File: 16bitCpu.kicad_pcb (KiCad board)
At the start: 2 copper layers, 12 parts, among them U1 74LS245, U10 74LS245, U11 74LS173, U12 74LS173, U2 74LS173, U3 74LS173, U4 74LS245, U5 74LS173, U6 74LS173, U7 74LS245, U8 74LS173, U9 74LS173

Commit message: Added IR,Cu started
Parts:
- added C1: 0.01uF, Capacitor_THT:CP_Axial_L10.0mm_D4.5mm_P15.00mm_Horizontal, F.Cu at (204.5, 35.6)
- added C2: 1uF, Capacitor_THT:CP_Axial_L10.0mm_D4.5mm_P15.00mm_Horizontal, F.Cu at (171.9, 55.0)
- added C3: 0.01uF, Capacitor_THT:CP_Axial_L10.0mm_D4.5mm_P15.00mm_Horizontal, F.Cu at (171.9, 61.5)
- added C4: 0.1uF, Capacitor_THT:CP_Axial_L10.0mm_D4.5mm_P15.00mm_Horizontal, F.Cu at (190.5, 55.0)
- added C5: 0.01uF, Capacitor_THT:CP_Axial_L10.0mm_D4.5mm_P15.00mm_Horizontal, F.Cu at (171.9, 68.0)
- added C6: 0.01uF, Capacitor_THT:CP_Axial_L10.0mm_D4.5mm_P15.00mm_Horizontal, F.Cu at (38.4, 118.4)
- added R1: 1K, Resistor_THT:R_Axial_DIN0204_L3.6mm_D1.6mm_P7.62mm_Horizontal, F.Cu at (207.2, 59.6)
- added R2: 1K, Resistor_THT:R_Axial_DIN0204_L3.6mm_D1.6mm_P7.62mm_Horizontal, F.Cu at (208.7, 53.1)
- added R3: 1K, Resistor_THT:R_Axial_DIN0204_L3.6mm_D1.6mm_P7.62mm_Horizontal, F.Cu at (214.8, 46.5)
- added R4: 1M, Resistor_THT:R_Axial_DIN0204_L3.6mm_D1.6mm_P7.62mm_Horizontal, F.Cu at (214.8, 43.3)
- added R5: 1K, Resistor_THT:R_Axial_DIN0204_L3.6mm_D1.6mm_P7.62mm_Horizontal, F.Cu at (214.8, 40.2)
- added R6: 1K, Resistor_THT:R_Axial_DIN0204_L3.6mm_D1.6mm_P7.62mm_Horizontal, F.Cu at (208.7, 50.0)
- added R7: 1K, Resistor_THT:R_Axial_DIN0204_L3.6mm_D1.6mm_P7.62mm_Horizontal, F.Cu at (56.6, 116.4)
- added RV1: 1M, ROM:Potentiometer-5.5mm, F.Cu at (205.1, 46.0)
- added SW1: SW_Push, Button_Switch_THT:SW_PUSH-12mm, F.Cu at (191.0, 62.3)
- added SW2: SW_SPDT, ROM:DPDT-pushbutton, F.Cu at (217.9, 58.8)
- added U13: 74LS173, Package_DIP:DIP-16_W7.62mm, F.Cu at (137.7, 114.2)
- added U14: 74LS245, Package_DIP:DIP-20_W7.62mm, F.Cu at (137.7, 135.9)
- added U15: 74LS173, Package_DIP:DIP-16_W7.62mm, F.Cu at (137.7, 103.4)
- added U16: 74LS173, Package_DIP:DIP-16_W7.62mm, F.Cu at (137.7, 92.5)
- added U17: 74LS245, Package_DIP:DIP-20_W7.62mm, F.Cu at (183.6, 102.2)
- added U18: 74LS173, Package_DIP:DIP-16_W7.62mm, F.Cu at (161.0, 106.0)
- added U19: 74LS173, Package_DIP:DIP-16_W7.62mm, F.Cu at (216.2, 102.2)
- added U20: 74LS245, Package_DIP:DIP-20_W7.62mm, F.Cu at (194.4, 102.2)
- added U21: 74LS173, Package_DIP:DIP-16_W7.62mm, F.Cu at (205.3, 102.2)
- added U22: 74LS173, Package_DIP:DIP-16_W7.62mm, F.Cu at (171.8, 106.0)
- added U23: LM555xM, Package_SO:SOIC-8_3.9x4.9mm_P1.27mm, F.Cu at (210.0, 64.4)
- added U24: 74LS04, Package_DIP:DIP-14_W7.62mm, F.Cu at (160.9, 34.1)
- added U25: 74LS08, Package_DIP:DIP-14_W7.62mm, F.Cu at (160.9, 53.5)
- added U26: 74LS04, Package_DIP:DIP-14_W7.62mm, F.Cu at (171.8, 34.1)
- added U27: 74LS32, Package_DIP:DIP-14_W7.62mm, F.Cu at (182.6, 34.1)
- added U28: LM555xM, Package_SO:SOIC-8_3.9x4.9mm_P1.27mm, F.Cu at (222.0, 51.3)
- added U29: 74LS04, Package_DIP:DIP-14_W7.62mm, F.Cu at (193.5, 34.1)
- added U30: LM555xM, Package_SO:SOIC-8_3.9x4.9mm_P1.27mm, F.Cu at (225.5, 35.3)
- added U31: 74LS245, Package_DIP:DIP-20_W7.62mm, F.Cu at (127.5, 34.1)
- added U32: 74HC04, Package_DIP:DIP-14_W7.62mm, F.Cu at (149.2, 34.1)
- added U33: 74LS173, Package_DIP:DIP-16_W7.62mm, F.Cu at (101.6, 71.3)
- added U34: 74HC00, Package_DIP:DIP-14_W7.62mm, F.Cu at (90.7, 93.2)
- added U35: 74LS173, Package_DIP:DIP-16_W7.62mm, F.Cu at (90.7, 71.3)
- added U36: 74LS245, Package_DIP:DIP-20_W7.62mm, F.Cu at (138.4, 34.1)
- added U37: 74LS173, Package_DIP:DIP-16_W7.62mm, F.Cu at (127.5, 61.1)
- added U38: 74LS173, Package_DIP:DIP-16_W7.62mm, F.Cu at (112.4, 71.3)
- added U39: AS6C6264, Package_DIP:DIP-28_W15.24mm, F.Cu at (90.7, 34.1)
- added U40: AS6C6264, Package_DIP:DIP-28_W15.24mm, F.Cu at (109.1, 34.1)
- added U41: AT28C64B-15PU, ROM:3M_240-1280-00-0602J, F.Cu at (51.3, 79.4)
- added U42: AT28C64B-15PU, ROM:3M_240-1280-00-0602J, F.Cu at (76.9, 79.4)
- added U43: 74LS245, Package_DIP:DIP-20_W7.62mm, F.Cu at (160.9, 77.8)
- added U44: 74LS245, Package_DIP:DIP-20_W7.62mm, F.Cu at (171.8, 77.8)
- added U45: 74LS161, Package_DIP:DIP-16_W7.62mm, F.Cu at (182.6, 77.8)
- added U46: 74LS161, Package_DIP:DIP-16_W7.62mm, F.Cu at (193.5, 77.8)
- added U47: 74LS161, Package_DIP:DIP-16_W7.62mm, F.Cu at (204.3, 77.8)
- added U48: 74LS161, Package_DIP:DIP-16_W7.62mm, F.Cu at (215.2, 77.8)
- U10, U7: value 74LS245 -> 74LS86; footprint Package_DIP:DIP-20_W7.62mm -> Package_DIP:DIP-14_W7.62mm
- U11, U2: value 74LS173 -> 74LS245; footprint Package_DIP:DIP-16_W7.62mm -> Package_DIP:DIP-20_W7.62mm
- U3, U5, U6: value 74LS173 -> 74LS283
- U4: value 74LS245 -> 74LS283; footprint Package_DIP:DIP-20_W7.62mm -> Package_DIP:DIP-16_W7.62mm
- U8, U9: value 74LS173 -> 74LS86; footprint Package_DIP:DIP-16_W7.62mm -> Package_DIP:DIP-14_W7.62mm
- moved U4 106.4 mm to (113.6, 137.5), turned to 90 degrees
- moved U5 105.4 mm to (113.6, 148.3), turned to 90 degrees
- moved U3 98.7 mm to (88.5, 143.3), turned to 90 degrees
- moved U2 97.2 mm to (57.7, 140.8), turned to 90 degrees
- moved U1 85.5 mm to (57.7, 130.0), turned to 90 degrees
- moved U6 82.4 mm to (113.6, 126.7), turned to 90 degrees
- moved U11 74.1 mm to (137.7, 146.8), turned to 90 degrees
- moved U7 59.2 mm to (88.5, 132.4), turned to 90 degrees
- moved U8 50.4 mm to (113.6, 115.8), turned to 90 degrees
- moved U12 50.4 mm to (137.7, 125.1), turned to 90 degrees
- moved U10 43.9 mm to (88.5, 121.6), turned to 90 degrees
- moved U9 35.3 mm to (113.6, 105.0), turned to 90 degrees
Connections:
- U1 pad 11: /register b/Bus5 -> /ALU/BUS7
- U1 pad 12: /register b/Bus6 -> /ALU/BUS6
- U1 pad 13: /register b/Bus5 -> /ALU/BUS5
- U1 pad 14: /register b/Bus4 -> /ALU/BUS4
- U1 pad 15: /register b/Bus12 -> /ALU/BUS3
- U1 pad 16: /register b/Bus2 -> /ALU/BUS2
- U1 pad 17: /register b/Bus1 -> /ALU/BUS1
- U1 pad 18: /register b/Bus0 -> /ALU/BUS0
- U1 pad 19: /resgister/AO -> /ALU/~EO
- U10 pad 1: +5V -> /sheet5F747766/A12
- U10 pad 10: GND -> /ALU/SU
- U10 pad 11: /register b/Bus15 -> Net-(U10-Pad11)
- U10 pad 12: /register b/Bus14 -> /sheet5F747766/A15
- U10 pad 13: /register b/Bus13 -> /ALU/SU
- U10 pad 14: /register b/Bus12 -> (no net)
- U10 pad 2: Net-(U10-Pad2) -> /ALU/SU
- U10 pad 4: Net-(U10-Pad4) -> /sheet5F747766/A13
- U10 pad 5: Net-(U10-Pad5) -> /ALU/SU
- U10 pad 7: Net-(U10-Pad7) -> (no net)
- U10 pad 9: Net-(U10-Pad9) -> /sheet5F747766/A14
- U11 pad 1: GND -> +5V
- U11 pad 10: /register b/AI -> GND
- U11 pad 11: /register b/Bus11 -> /ALU/BUS7
- U11 pad 12: /register b/Bus10 -> /ALU/BUS6
- U11 pad 13: /register b/Bus9 -> /ALU/BUS5
- U11 pad 14: /register b/Bus8 -> /ALU/BUS4
- U11 pad 15: /register b/CLR -> /ALU/BUS3
- U11 pad 16: +5V -> /ALU/BUS2
- U11 pad 2: GND -> /ALU/A0
- U11 pad 3: Net-(U10-Pad2) -> /ALU/A1
- U11 pad 4: Net-(U10-Pad3) -> /ALU/A2
- U11 pad 5: Net-(U10-Pad4) -> /ALU/A3
- U11 pad 6: Net-(U10-Pad5) -> /ALU/A4
- U11 pad 7: /register b/CLK -> /ALU/A5
- U11 pad 8: GND -> /ALU/A6
- U11 pad 9: /register b/AI -> /ALU/A7
- U12 pad 10: /register b/AI -> /Resgister A/~AI
- U12 pad 11: /register b/Bus15 -> /ALU/BUS3
- U12 pad 12: /register b/Bus14 -> /ALU/BUS2
- U12 pad 13: /register b/Bus13 -> /ALU/BUS1
- U12 pad 14: /register b/Bus12 -> /ALU/BUS0
- U12 pad 15: /register b/CLR -> /Resgister A/CLR
- U12 pad 3: Net-(U10-Pad6) -> /ALU/A0
- U12 pad 4: Net-(U10-Pad7) -> /ALU/A1
- U12 pad 5: Net-(U10-Pad8) -> /ALU/A2
- U12 pad 6: Net-(U10-Pad9) -> /ALU/A3
- U12 pad 7: /register b/CLK -> /ProgramCounter/CLK
- U12 pad 9: /register b/AI -> /Resgister A/~AI
- U2 pad 1: GND -> +5V
- U2 pad 10: /resgister/AI -> GND
- U2 pad 11: /register b/Bus12 -> /ALU/BUS13
- U2 pad 12: /register b/Bus2 -> /ALU/BUS14
- U2 pad 13: /register b/Bus1 -> /ALU/BUS13
- U2 pad 14: /register b/Bus0 -> /ALU/BUS12
- U2 pad 15: /resgister/CLR -> /ALU/BUS11
- U2 pad 16: +5V -> /ALU/BUS10
- U2 pad 2: GND -> Net-(U2-Pad2)
- U2 pad 3: Net-(U1-Pad2) -> Net-(U2-Pad3)
- U2 pad 4: Net-(U1-Pad3) -> Net-(U2-Pad4)
- U2 pad 5: Net-(U1-Pad4) -> Net-(U2-Pad5)
- U2 pad 6: Net-(U1-Pad5) -> Net-(U2-Pad6)
- U2 pad 7: /resgister/CLK -> Net-(U2-Pad7)
- U2 pad 8: GND -> Net-(U2-Pad8)
- U2 pad 9: /resgister/AI -> Net-(U2-Pad9)
- U3 pad 1: GND -> Net-(U1-Pad3)
- U3 pad 10: /resgister/AI -> Net-(U1-Pad5)
- U3 pad 11: /register b/Bus5 -> Net-(U3-Pad11)
- U3 pad 12: /register b/Bus6 -> /ALU/A3
- U3 pad 13: /register b/Bus5 -> Net-(U1-Pad4)
- U3 pad 14: /register b/Bus4 -> /ALU/A2
- U3 pad 15: /resgister/CLR -> Net-(U3-Pad15)
- U3 pad 2: GND -> Net-(U3-Pad2)
- U3 pad 3: Net-(U1-Pad6) -> /ALU/A1
- U3 pad 4: Net-(U1-Pad7) -> Net-(U1-Pad2)
- U3 pad 5: Net-(U1-Pad8) -> /ALU/A0
- U3 pad 6: Net-(U1-Pad9) -> Net-(U3-Pad6)
- U3 pad 7: /resgister/CLK -> /ALU/SU
- U3 pad 9: /resgister/AI -> Net-(U3-Pad9)
- U4 pad 1: +5V -> Net-(U2-Pad3)
- U4 pad 10: GND -> Net-(U2-Pad5)
- U4 pad 11: /register b/Bus15 -> Net-(U4-Pad11)
- U4 pad 12: /register b/Bus14 -> /ALU/A11
- U4 pad 13: /register b/Bus13 -> Net-(U2-Pad4)
- U4 pad 14: /register b/Bus12 -> /ALU/A10
- U4 pad 15: /register b/Bus11 -> Net-(U4-Pad15)
- U4 pad 16: /register b/Bus10 -> +5V
- U4 pad 3: Net-(U4-Pad3) -> /ALU/A9
- U4 pad 4: Net-(U4-Pad4) -> Net-(U2-Pad2)
- U4 pad 5: Net-(U4-Pad5) -> /ALU/A8
- U4 pad 8: Net-(U4-Pad8) -> GND
- U5 pad 1: GND -> Net-(U1-Pad7)
- U5 pad 10: /resgister/AI -> Net-(U1-Pad9)
- U5 pad 11: /register b/Bus11 -> Net-(U5-Pad11)
- U5 pad 12: /register b/Bus10 -> /ALU/A7
- U5 pad 13: /register b/Bus9 -> Net-(U1-Pad8)
- U5 pad 14: /register b/Bus8 -> /ALU/A6
- U5 pad 15: /resgister/CLR -> Net-(U5-Pad15)
- U5 pad 2: GND -> Net-(U5-Pad2)
- U5 pad 3: Net-(U4-Pad2) -> /ALU/A5
- U5 pad 4: Net-(U4-Pad3) -> Net-(U1-Pad6)
- U5 pad 5: Net-(U4-Pad4) -> /ALU/A4
- U5 pad 6: Net-(U4-Pad5) -> Net-(U5-Pad6)
- U5 pad 7: /resgister/CLK -> Net-(U3-Pad9)
- U5 pad 9: /resgister/AI -> Net-(U4-Pad7)
- U6 pad 1: GND -> Net-(U2-Pad7)
- U6 pad 10: /resgister/AI -> Net-(U2-Pad9)
- U6 pad 11: /register b/Bus15 -> Net-(U10-Pad11)
- U6 pad 12: /register b/Bus14 -> /ALU/A15
- U6 pad 13: /register b/Bus13 -> Net-(U2-Pad8)
- U6 pad 14: /register b/Bus12 -> /ALU/A14
- U6 pad 15: /resgister/CLR -> Net-(U10-Pad8)
- U6 pad 2: GND -> Net-(U10-Pad6)
- U6 pad 3: Net-(U4-Pad6) -> /ALU/A13
- U6 pad 4: Net-(U4-Pad7) -> Net-(U2-Pad6)
- U6 pad 5: Net-(U4-Pad8) -> /ALU/A12
- U6 pad 6: Net-(U4-Pad9) -> Net-(U10-Pad3)
- U6 pad 7: /resgister/CLK -> Net-(U4-Pad9)
- U6 pad 9: /resgister/AI -> (no net)
- U7 pad 1: +5V -> /sheet5F747766/A0
- U7 pad 10: GND -> /ALU/SU
- U7 pad 11: /register b/Bus5 -> Net-(U3-Pad11)
- U7 pad 12: /register b/Bus6 -> /sheet5F747766/A3
- U7 pad 13: /register b/Bus5 -> /ALU/SU
- U7 pad 14: /register b/Bus4 -> (no net)
- U7 pad 2: Net-(U7-Pad2) -> /ALU/SU
- U7 pad 3: Net-(U7-Pad3) -> Net-(U3-Pad6)
- U7 pad 4: Net-(U7-Pad4) -> /sheet5F747766/A1
- U7 pad 5: Net-(U7-Pad5) -> /ALU/SU
- U7 pad 6: Net-(U7-Pad6) -> Net-(U3-Pad2)
- U7 pad 7: Net-(U7-Pad7) -> (no net)
- U7 pad 8: Net-(U7-Pad8) -> Net-(U3-Pad15)
- U7 pad 9: Net-(U7-Pad9) -> /sheet5F747766/A2
- U8 pad 1: GND -> /sheet5F747766/A4
- U8 pad 10: /register b/AI -> /ALU/SU
- U8 pad 11: /register b/Bus12 -> Net-(U5-Pad11)
- U8 pad 12: /register b/Bus2 -> /sheet5F747766/A7
- U8 pad 13: /register b/Bus1 -> /ALU/SU
- U8 pad 14: /register b/Bus0 -> (no net)
- U8 pad 2: GND -> /ALU/SU
- U8 pad 3: Net-(U7-Pad2) -> Net-(U5-Pad6)
- U8 pad 4: Net-(U7-Pad3) -> /sheet5F747766/A5
- U8 pad 5: Net-(U7-Pad4) -> /ALU/SU
- U8 pad 6: Net-(U7-Pad5) -> Net-(U5-Pad2)
- U8 pad 7: /register b/CLK -> (no net)
- U8 pad 8: GND -> Net-(U5-Pad15)
- U8 pad 9: /register b/AI -> /sheet5F747766/A6
- U9 pad 1: GND -> /sheet5F747766/A8
- U9 pad 10: /register b/AI -> /ALU/SU
- U9 pad 11: /register b/Bus5 -> Net-(U4-Pad11)
- U9 pad 12: /register b/Bus6 -> /sheet5F747766/A11
- U9 pad 13: /register b/Bus5 -> /ALU/SU
- U9 pad 14: /register b/Bus4 -> (no net)
- U9 pad 2: GND -> /ALU/SU
- U9 pad 3: Net-(U7-Pad6) -> Net-(U4-Pad6)
- U9 pad 4: Net-(U7-Pad7) -> /sheet5F747766/A9
- U9 pad 5: Net-(U7-Pad8) -> /ALU/SU
- U9 pad 6: Net-(U7-Pad9) -> Net-(U4-Pad2)
- U9 pad 7: /register b/CLK -> (no net)
- U9 pad 8: GND -> Net-(U4-Pad15)
- U9 pad 9: /register b/AI -> /sheet5F747766/A10
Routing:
- net GND: track 0.00 -> 793.5 mm
- net +5V: track 0.00 -> 678.2 mm
- net /ALU/BUS12: track 0.00 -> 433.3 mm, vias 0 -> 1
- net /ALU/BUS13: track 0.00 -> 427.8 mm, vias 0 -> 1
- net /ALU/BUS8: track 0.00 -> 398.9 mm, vias 0 -> 1
- net /ALU/BUS14: track 0.00 -> 395.8 mm
- net /ALU/BUS5: track 0.00 -> 395.0 mm, vias 0 -> 3
- net /ALU/BUS10: track 0.00 -> 382.4 mm, vias 0 -> 3
- net /ALU/BUS6: track 0.00 -> 377.8 mm, vias 0 -> 2
- net /ALU/BUS11: track 0.00 -> 377.0 mm
- net /ALU/BUS9: track 0.00 -> 375.2 mm, vias 0 -> 1
- net /ALU/BUS4: track 0.00 -> 353.2 mm, vias 0 -> 5
- net /ProgramCounter/CLK: track 0.00 -> 351.4 mm
- net /ALU/BUS7: track 0.00 -> 346.4 mm, vias 0 -> 1
- net /ALU/BUS0: track 0.00 -> 338.1 mm
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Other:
- copper layers 2 -> 4

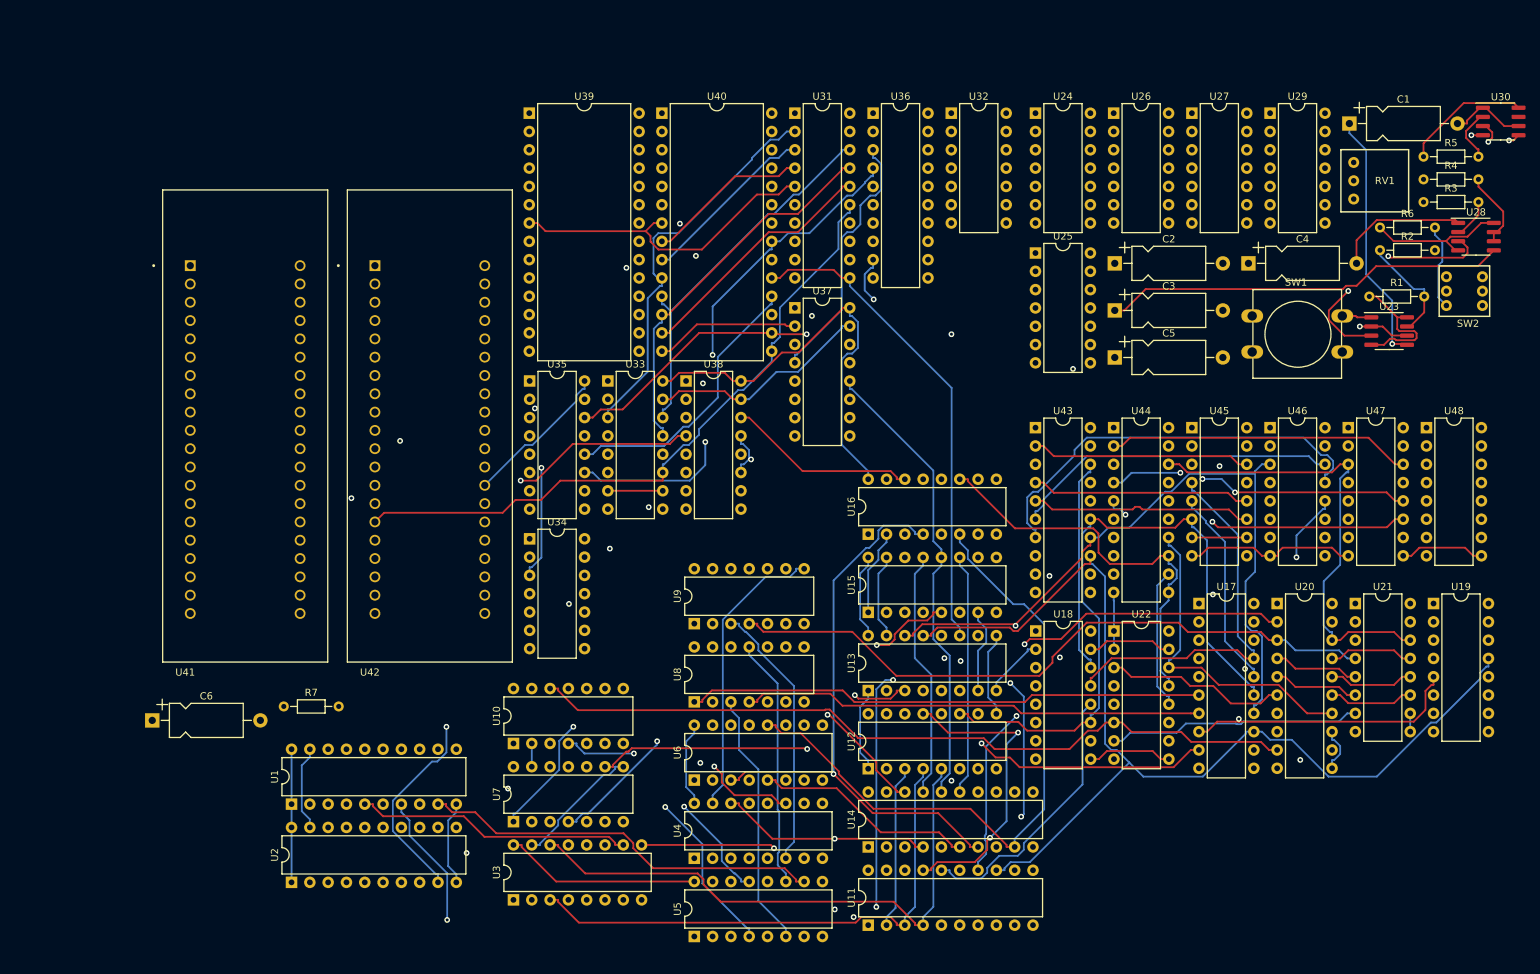
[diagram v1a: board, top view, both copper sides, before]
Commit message: Fixed power for multi part comps
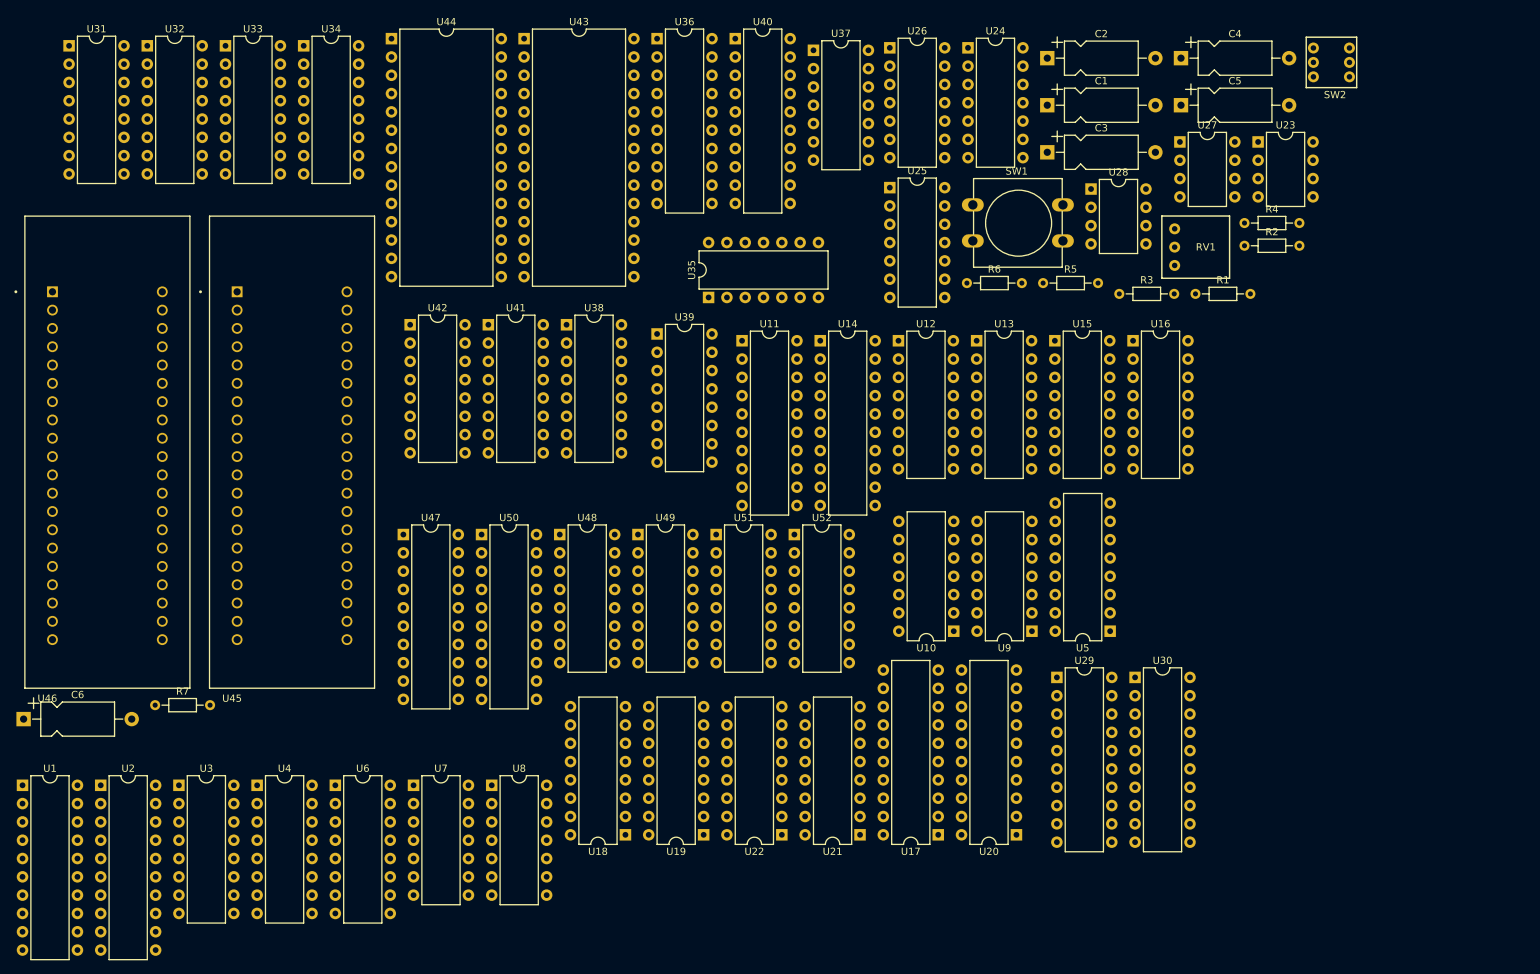
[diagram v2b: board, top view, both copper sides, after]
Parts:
- removed the U48 at (215.2, 77.8)
- added R4: 1M, Resistor_THT:R_Axial_DIN0204_L3.6mm_D1.6mm_P7.62mm_Horizontal, F.Cu at (189.9, 49.4)
- added U49: 74LS173, Package_DIP:DIP-16_W7.62mm, F.Cu at (105.8, 92.6)
- added U50: 74LS245, Package_DIP:DIP-20_W7.62mm, F.Cu at (84.1, 92.6)
- added U51: 74LS173, Package_DIP:DIP-16_W7.62mm, F.Cu at (116.6, 92.6)
- added U52: 74LS173, Package_DIP:DIP-16_W7.62mm, F.Cu at (127.5, 92.6)
- U23, U28: value LM555xM -> LM555xN; footprint Package_SO:SOIC-8_3.9x4.9mm_P1.27mm -> Package_DIP:DIP-8_W7.62mm
- U24, U26: value 74LS04 -> 74LS08
- U27: value 74LS32 -> LM555xN; footprint Package_DIP:DIP-14_W7.62mm -> Package_DIP:DIP-8_W7.62mm
- U29: value 74LS04 -> 74LS245; footprint Package_DIP:DIP-14_W7.62mm -> Package_DIP:DIP-20_W7.62mm
- U30: value LM555xM -> 74LS245; footprint Package_SO:SOIC-8_3.9x4.9mm_P1.27mm -> Package_DIP:DIP-20_W7.62mm
- U31: value 74LS245 -> 74LS161; footprint Package_DIP:DIP-20_W7.62mm -> Package_DIP:DIP-16_W7.62mm
- U32: value 74HC04 -> 74LS161; footprint Package_DIP:DIP-14_W7.62mm -> Package_DIP:DIP-16_W7.62mm
- U33: value 74LS173 -> 74LS161
- U34: value 74HC00 -> 74LS161; footprint Package_DIP:DIP-14_W7.62mm -> Package_DIP:DIP-16_W7.62mm
- U35: value 74LS173 -> 74HC00; footprint Package_DIP:DIP-16_W7.62mm -> Package_DIP:DIP-14_W7.62mm
- U37: value 74LS173 -> 74HC04; footprint Package_DIP:DIP-16_W7.62mm -> Package_DIP:DIP-14_W7.62mm
- U39: value AS6C6264 -> 74LS173; footprint Package_DIP:DIP-28_W15.24mm -> Package_DIP:DIP-16_W7.62mm
- U40: value AS6C6264 -> 74LS245; footprint Package_DIP:DIP-28_W15.24mm -> Package_DIP:DIP-20_W7.62mm
- U41, U42: value AT28C64B-15PU -> 74LS173; footprint ROM:3M_240-1280-00-0602J -> Package_DIP:DIP-16_W7.62mm
- U43, U44: value 74LS245 -> AS6C6264; footprint Package_DIP:DIP-20_W7.62mm -> Package_DIP:DIP-28_W15.24mm
- U45, U46: value 74LS161 -> AT28C64B-15PU; footprint Package_DIP:DIP-16_W7.62mm -> ROM:3M_240-1280-00-0602J
- U47: value 74LS161 -> 74LS245; footprint Package_DIP:DIP-16_W7.62mm -> Package_DIP:DIP-20_W7.62mm
- U48: renamed from R4; value 1M -> 74LS173; footprint Resistor_THT:R_Axial_DIN0204_L3.6mm_D1.6mm_P7.62mm_Horizontal -> Package_DIP:DIP-16_W7.62mm
- moved U46 161.4 mm to (32.2, 83.0)
- moved U47 131.9 mm to (73.2, 92.6)
- moved U48 129.6 mm to (94.9, 92.6)
- moved U45 125.0 mm to (57.8, 83.0)
- moved U44 113.8 mm to (71.6, 23.8)
- moved U32 111.9 mm to (37.7, 24.8)
- moved U19 106.2 mm to (114.9, 134.2), turned to 180 degrees
- moved U31 101.1 mm to (26.8, 24.8)
- moved U30 92.3 mm to (174.7, 112.4)
- moved U43 89.1 mm to (90.0, 23.8)
- moved U29 83.7 mm to (163.9, 112.4)
- moved U11 83.0 mm to (120.2, 65.7), turned to 0 degrees
- moved U21 75.8 mm to (136.6, 134.2), turned to 180 degrees
- moved U34 75.2 mm to (59.4, 24.8)
- moved U5 71.6 mm to (171.3, 106.0), turned to 180 degrees
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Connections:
- RV1 pad 3: (no net) -> Net-(RV1-Pad3)
- U10 pad 14: (no net) -> +5V
- U10 pad 7: (no net) -> GND
- U12 pad 7: /ProgramCounter/CLK -> /Control Unit/CLK
- U13 pad 7: /ProgramCounter/CLK -> /Control Unit/CLK
- U14 pad 11: /ALU/BUS13 -> /ALU/BUS15
- U15 pad 7: /ProgramCounter/CLK -> /Control Unit/CLK
- U16 pad 11: /ALU/BUS13 -> /ALU/BUS15
- U16 pad 7: /ProgramCounter/CLK -> /Control Unit/CLK
- U18 pad 7: /ProgramCounter/CLK -> /Control Unit/CLK
- U19 pad 7: /ProgramCounter/CLK -> /Control Unit/CLK
- U2 pad 11: /ALU/BUS13 -> /ALU/BUS15
- U20 pad 11: /ALU/BUS13 -> /ALU/BUS15
- U21 pad 7: /ProgramCounter/CLK -> /Control Unit/CLK
- U22 pad 11: /ALU/BUS13 -> /ALU/BUS15
- U22 pad 7: /ProgramCounter/CLK -> /Control Unit/CLK
- U24 pad 14: (no net) -> +5V
- U24 pad 3: (no net) -> /clock/HLT
- U24 pad 4: (no net) -> Net-(U24-Pad4)
- U24 pad 5: (no net) -> /Control Unit/CLK
- U24 pad 6: (no net) -> /clock/~CLK
- U24 pad 7: (no net) -> GND
- U25 pad 10: Net-(U25-Pad10) -> Net-(U24-Pad4)
- U25 pad 14: (no net) -> +5V
- U25 pad 7: (no net) -> GND
- U25 pad 8: /ProgramCounter/CLK -> /Control Unit/CLK
- U26 pad 1: (no net) -> Net-(U25-Pad3)
- U26 pad 14: (no net) -> +5V
- U26 pad 2: Net-(U25-Pad10) -> Net-(U25-Pad6)
- U26 pad 3: (no net) -> Net-(U25-Pad9)
- U26 pad 7: (no net) -> GND
- U27 pad 1: Net-(U25-Pad3) -> GND
- U27 pad 2: Net-(U25-Pad6) -> Net-(R3-Pad2)
- U27 pad 3: Net-(U25-Pad9) -> Net-(U25-Pad5)
- U27 pad 4: (no net) -> +5V
- U27 pad 5: (no net) -> Net-(C3-Pad1)
- U27 pad 6: (no net) -> Net-(C4-Pad1)
- U27 pad 7: (no net) -> Net-(C4-Pad1)
- U27 pad 8: (no net) -> +5V
- U28 pad 2: Net-(R3-Pad2) -> Net-(R5-Pad2)
- U28 pad 3: Net-(U25-Pad5) -> Net-(U24-Pad1)
- U28 pad 4: +5V -> Net-(R6-Pad2)
- U28 pad 5: Net-(C3-Pad1) -> Net-(C5-Pad1)
- U28 pad 6: Net-(C4-Pad1) -> GND
- U28 pad 7: Net-(C4-Pad1) -> Net-(U28-Pad7)
- U29 pad 1: /ProgramCounter/CLK -> +5V
- U29 pad 10: (no net) -> GND
- U29 pad 11: (no net) -> /ALU/BUS7
- U29 pad 12: (no net) -> /ALU/BUS6
- U29 pad 13: (no net) -> /ALU/BUS5
- U29 pad 14: (no net) -> /ALU/BUS4
- U29 pad 2: (no net) -> Net-(U29-Pad2)
- U29 pad 3: (no net) -> Net-(U29-Pad3)
- U29 pad 4: (no net) -> Net-(U29-Pad4)
- U29 pad 5: (no net) -> Net-(U29-Pad5)
- U29 pad 6: (no net) -> Net-(U29-Pad6)
- U29 pad 7: (no net) -> Net-(U29-Pad7)
- U29 pad 8: (no net) -> Net-(U29-Pad8)
- U29 pad 9: (no net) -> Net-(U29-Pad9)
- U30 pad 1: GND -> +5V
- U30 pad 2: Net-(R5-Pad2) -> Net-(U30-Pad2)
- U30 pad 3: Net-(U24-Pad1) -> Net-(U30-Pad3)
- U30 pad 4: Net-(R6-Pad2) -> Net-(U30-Pad4)
- U30 pad 5: Net-(C5-Pad1) -> Net-(U30-Pad5)
- U30 pad 6: GND -> Net-(U30-Pad6)
- U30 pad 7: (no net) -> Net-(U30-Pad7)
- U30 pad 8: +5V -> Net-(U30-Pad8)
- U31 pad 1: +5V -> /ProgramCounter/~CLR
- U31 pad 10: GND -> /ProgramCounter/CE
- U31 pad 11: /ALU/BUS7 -> Net-(U29-Pad5)
- U31 pad 12: /ALU/BUS6 -> Net-(U29-Pad4)
- U31 pad 13: /ALU/BUS5 -> Net-(U29-Pad3)
- U31 pad 14: /ALU/BUS4 -> Net-(U29-Pad2)
- U31 pad 15: /ALU/BUS3 -> Net-(U31-Pad15)
- U31 pad 16: /ALU/BUS2 -> +5V
- U31 pad 2: Net-(U31-Pad2) -> /Control Unit/CLK
- U31 pad 3: Net-(U31-Pad3) -> /ALU/BUS0
- U31 pad 4: Net-(U31-Pad4) -> /ALU/BUS1
- U31 pad 5: Net-(U31-Pad5) -> /ALU/BUS2
- U31 pad 6: Net-(U31-Pad6) -> /ALU/BUS3
- U31 pad 7: Net-(U31-Pad7) -> /ProgramCounter/CE
- U31 pad 8: Net-(U31-Pad8) -> GND
- U31 pad 9: Net-(U31-Pad9) -> /ProgramCounter/~J
- U32 pad 1: /ProgramCounter/CLK -> /ProgramCounter/~CLR
- U32 pad 10: (no net) -> /ProgramCounter/CE
- U32 pad 11: (no net) -> Net-(U29-Pad9)
- U32 pad 12: (no net) -> Net-(U29-Pad8)
- U32 pad 13: (no net) -> Net-(U29-Pad7)
- U32 pad 14: (no net) -> Net-(U29-Pad6)
- U32 pad 2: Net-(U32-Pad2) -> Net-(U31-Pad15)
- U32 pad 3: Net-(U32-Pad2) -> /ALU/BUS4
- U32 pad 4: Net-(C6-Pad1) -> /ALU/BUS5
- U32 pad 5: (no net) -> /ALU/BUS6
- U32 pad 6: (no net) -> /ALU/BUS7
- U32 pad 7: (no net) -> /ProgramCounter/CE
- U32 pad 8: (no net) -> GND
- U32 pad 9: (no net) -> /ProgramCounter/~J
- U33 pad 1: GND -> /ProgramCounter/~CLR
- U33 pad 10: /ProgramCounter/CLK -> /ProgramCounter/CE
- U33 pad 11: /ALU/BUS3 -> Net-(U30-Pad5)
- U33 pad 12: /ALU/BUS2 -> Net-(U30-Pad4)
- U33 pad 13: /ALU/BUS1 -> Net-(U30-Pad3)
- U33 pad 14: /ALU/BUS0 -> Net-(U30-Pad2)
- U33 pad 15: /RAM/CLR -> Net-(U33-Pad15)
- U33 pad 2: GND -> Net-(U32-Pad15)
- U33 pad 3: Net-(U31-Pad2) -> /ALU/BUS8
- U33 pad 4: Net-(U31-Pad3) -> /ALU/BUS9
- U33 pad 5: Net-(U31-Pad4) -> /ALU/BUS10
- U33 pad 6: Net-(U31-Pad5) -> /ALU/BUS11
- U33 pad 7: /ProgramCounter/CLK -> /ProgramCounter/CE
- U33 pad 9: /ProgramCounter/CLK -> /ProgramCounter/~J
- U34 pad 1: (no net) -> /ProgramCounter/~CLR
- U34 pad 10: (no net) -> /ProgramCounter/CE
- U34 pad 11: (no net) -> Net-(U30-Pad9)
- U34 pad 12: (no net) -> Net-(U30-Pad8)
- U34 pad 13: (no net) -> Net-(U30-Pad7)
- U34 pad 14: (no net) -> Net-(U30-Pad6)
- U34 pad 2: Net-(C6-Pad2) -> Net-(U33-Pad15)
- U34 pad 3: Net-(U34-Pad3) -> /ALU/BUS12
- U34 pad 4: (no net) -> /ALU/BUS13
- U34 pad 5: (no net) -> /ALU/BUS14
- U34 pad 6: (no net) -> /ALU/BUS15
- U34 pad 7: (no net) -> /ProgramCounter/CE
- U34 pad 8: (no net) -> GND
- U34 pad 9: (no net) -> /ProgramCounter/~J
- U35 pad 1: GND -> /RAM/MEMWE
- U35 pad 10: /ProgramCounter/CLK -> (no net)
- U35 pad 11: /ALU/BUS7 -> (no net)
- U35 pad 12: /ALU/BUS6 -> (no net)
- U35 pad 13: /ALU/BUS5 -> (no net)
- U35 pad 14: /ALU/BUS4 -> +5V
- U35 pad 2: GND -> Net-(C6-Pad2)
- U35 pad 3: Net-(U31-Pad6) -> Net-(U35-Pad3)
- U35 pad 4: Net-(U31-Pad7) -> (no net)
- U35 pad 5: Net-(U31-Pad8) -> (no net)
- U35 pad 6: Net-(U31-Pad9) -> (no net)
- U35 pad 7: /ProgramCounter/CLK -> GND
- U35 pad 8: GND -> (no net)
- U35 pad 9: /ProgramCounter/CLK -> (no net)
- U36 pad 11: /ALU/BUS13 -> /ALU/BUS7
- U36 pad 12: /ALU/BUS14 -> /ALU/BUS6
- U36 pad 13: /ALU/BUS13 -> /ALU/BUS5
- U36 pad 14: /ALU/BUS12 -> /ALU/BUS4
- U36 pad 15: /ALU/BUS11 -> /ALU/BUS3
- U36 pad 16: /ALU/BUS10 -> /ALU/BUS2
- U36 pad 17: /ALU/BUS9 -> /ALU/BUS1
- U36 pad 18: /ALU/BUS8 -> /ALU/BUS0
- U36 pad 7: /RAM/A13 -> Net-(U36-Pad7)
- U36 pad 8: /RAM/A14 -> Net-(U36-Pad8)
- U36 pad 9: /RAM/A15 -> Net-(U36-Pad9)
- U37 pad 1: GND -> /Control Unit/CLK
- U37 pad 10: /ProgramCounter/CLK -> (no net)
- U37 pad 11: /ALU/BUS11 -> (no net)
- U37 pad 12: /ALU/BUS10 -> (no net)
- U37 pad 13: /ALU/BUS9 -> (no net)
- U37 pad 14: /ALU/BUS8 -> +5V
- U37 pad 2: GND -> Net-(U37-Pad2)
- U37 pad 3: Net-(U36-Pad2) -> Net-(U37-Pad2)
- U37 pad 4: Net-(U36-Pad3) -> Net-(C6-Pad1)
- U37 pad 5: Net-(U36-Pad4) -> (no net)
- U37 pad 6: Net-(U36-Pad5) -> (no net)
- U37 pad 7: /ProgramCounter/CLK -> GND
- U37 pad 8: GND -> (no net)
- U37 pad 9: /ProgramCounter/CLK -> (no net)
- U38 pad 10: /ProgramCounter/CLK -> /RAM/~AI
- U38 pad 11: /ALU/BUS13 -> /ALU/BUS3
- U38 pad 12: /ALU/BUS14 -> /ALU/BUS2
- U38 pad 13: /ALU/BUS13 -> /ALU/BUS1
- U38 pad 14: /ALU/BUS12 -> /ALU/BUS0
- U38 pad 3: Net-(U36-Pad6) -> Net-(U36-Pad2)
- U38 pad 4: /RAM/A13 -> Net-(U36-Pad3)
- U38 pad 5: /RAM/A14 -> Net-(U36-Pad4)
- U38 pad 6: /RAM/A15 -> Net-(U36-Pad5)
- U38 pad 7: /ProgramCounter/CLK -> /Control Unit/CLK
- U38 pad 9: /ProgramCounter/CLK -> /RAM/~AI
- U39 pad 1: (no net) -> GND
- U39 pad 10: Net-(U31-Pad2) -> /RAM/~AI
- U39 pad 11: /ALU/BUS8 -> /ALU/BUS7
- U39 pad 12: /ALU/BUS9 -> /ALU/BUS6
- U39 pad 13: /ALU/BUS10 -> /ALU/BUS5
- U39 pad 14: GND -> /ALU/BUS4
- U39 pad 15: /ALU/BUS11 -> /RAM/CLR
- U39 pad 16: /ALU/BUS12 -> +5V
- U39 pad 2: Net-(U36-Pad6) -> GND
- U39 pad 3: Net-(U31-Pad9) -> Net-(U36-Pad6)
- U39 pad 4: Net-(U31-Pad8) -> Net-(U36-Pad7)
- U39 pad 5: Net-(U31-Pad7) -> Net-(U36-Pad8)
- U39 pad 6: Net-(U31-Pad6) -> Net-(U36-Pad9)
- U39 pad 7: Net-(U31-Pad5) -> /Control Unit/CLK
- U39 pad 8: Net-(U31-Pad4) -> GND
- U39 pad 9: Net-(U31-Pad3) -> /RAM/~AI
- U40 pad 1: (no net) -> +5V
- U40 pad 10: Net-(U31-Pad2) -> GND
- U40 pad 11: /ALU/BUS0 -> /ALU/BUS15
- U40 pad 12: /ALU/BUS1 -> /ALU/BUS14
- U40 pad 13: /ALU/BUS2 -> /ALU/BUS13
- U40 pad 14: GND -> /ALU/BUS12
- U40 pad 15: /ALU/BUS3 -> /ALU/BUS11
- U40 pad 16: /ALU/BUS4 -> /ALU/BUS10
- U40 pad 17: /ALU/BUS5 -> /ALU/BUS9
- U40 pad 18: /ALU/BUS6 -> /ALU/BUS8
- U40 pad 19: /ALU/BUS7 -> /RAM/~AO
- U40 pad 2: Net-(U36-Pad6) -> Net-(U40-Pad2)
- U40 pad 20: GND -> +5V
- U40 pad 3: Net-(U31-Pad9) -> Net-(U40-Pad3)
- U40 pad 4: Net-(U31-Pad8) -> Net-(U40-Pad4)
- U40 pad 5: Net-(U31-Pad7) -> Net-(U40-Pad5)
- U40 pad 6: Net-(U31-Pad6) -> Net-(U40-Pad6)
- U40 pad 7: Net-(U31-Pad5) -> /RAM/A13
- U40 pad 8: Net-(U31-Pad4) -> /RAM/A14
- U40 pad 9: Net-(U31-Pad3) -> /RAM/A15
- U41 pad 1: (no net) -> GND
- U41 pad 10: Net-(U31-Pad2) -> /RAM/~AI
- U41 pad 11: /ALU/BUS8 -> /ALU/BUS11
- U41 pad 12: /ALU/BUS9 -> /ALU/BUS10
- U41 pad 13: /ALU/BUS10 -> /ALU/BUS9
- U41 pad 14: GND -> /ALU/BUS8
- U41 pad 15: /ALU/BUS11 -> /RAM/CLR
- U41 pad 16: /ALU/BUS12 -> +5V
- U41 pad 2: Net-(U36-Pad6) -> GND
- U41 pad 3: Net-(U31-Pad9) -> Net-(U40-Pad2)
- U41 pad 4: Net-(U31-Pad8) -> Net-(U40-Pad3)
- U41 pad 5: Net-(U31-Pad7) -> Net-(U40-Pad4)
- U41 pad 6: Net-(U31-Pad6) -> Net-(U40-Pad5)
- U41 pad 7: Net-(U31-Pad5) -> /Control Unit/CLK
- U41 pad 8: Net-(U31-Pad4) -> GND
- U41 pad 9: Net-(U31-Pad3) -> /RAM/~AI
- U42 pad 1: (no net) -> GND
- U42 pad 10: Net-(U31-Pad2) -> /RAM/~AI
- U42 pad 11: /ALU/BUS0 -> /ALU/BUS15
- U42 pad 12: /ALU/BUS1 -> /ALU/BUS14
- U42 pad 13: /ALU/BUS2 -> /ALU/BUS13
- U42 pad 14: GND -> /ALU/BUS12
- U42 pad 15: /ALU/BUS3 -> /RAM/CLR
- U42 pad 16: /ALU/BUS4 -> +5V
- U42 pad 2: Net-(U36-Pad6) -> GND
- U42 pad 3: Net-(U31-Pad9) -> Net-(U40-Pad6)
- U42 pad 4: Net-(U31-Pad8) -> /RAM/A13
- U42 pad 5: Net-(U31-Pad7) -> /RAM/A14
- U42 pad 6: Net-(U31-Pad6) -> /RAM/A15
- U42 pad 7: Net-(U31-Pad5) -> /Control Unit/CLK
- U42 pad 8: Net-(U31-Pad4) -> GND
- U42 pad 9: Net-(U31-Pad3) -> /RAM/~AI
- U43 pad 1: +5V -> Net-(U43-Pad1)
- U43 pad 10: GND -> Net-(U36-Pad2)
- U43 pad 11: /ALU/BUS7 -> /ALU/BUS8
- U43 pad 12: /ALU/BUS6 -> /ALU/BUS9
- U43 pad 13: /ALU/BUS5 -> /ALU/BUS10
- U43 pad 14: /ALU/BUS4 -> GND
- U43 pad 15: /ALU/BUS3 -> /ALU/BUS11
- U43 pad 16: /ALU/BUS2 -> /ALU/BUS12
- U43 pad 17: /ALU/BUS1 -> /ALU/BUS13
- U43 pad 18: /ALU/BUS0 -> /ALU/BUS14
- U43 pad 19: /ProgramCounter/~CO -> /ALU/BUS15
- U43 pad 2: Net-(U43-Pad2) -> Net-(U40-Pad6)
- U43 pad 20: +5V -> GND
- U43 pad 3: Net-(U43-Pad3) -> Net-(U36-Pad9)
- U43 pad 4: Net-(U43-Pad4) -> Net-(U36-Pad8)
- U43 pad 5: Net-(U43-Pad5) -> Net-(U36-Pad7)
- U43 pad 6: Net-(U43-Pad6) -> Net-(U36-Pad6)
- U43 pad 7: Net-(U43-Pad7) -> Net-(U36-Pad5)
- U43 pad 8: Net-(U43-Pad8) -> Net-(U36-Pad4)
- U43 pad 9: Net-(U43-Pad9) -> Net-(U36-Pad3)
- U44 pad 1: +5V -> Net-(U44-Pad1)
- U44 pad 10: GND -> Net-(U36-Pad2)
- U44 pad 11: /ALU/BUS13 -> /ALU/BUS0
- U44 pad 12: /ALU/BUS14 -> /ALU/BUS1
- U44 pad 13: /ALU/BUS13 -> /ALU/BUS2
- U44 pad 14: /ALU/BUS12 -> GND
- U44 pad 15: /ALU/BUS11 -> /ALU/BUS3
- U44 pad 16: /ALU/BUS10 -> /ALU/BUS4
- U44 pad 17: /ALU/BUS9 -> /ALU/BUS5
- U44 pad 18: /ALU/BUS8 -> /ALU/BUS6
- U44 pad 19: /ProgramCounter/~CO -> /ALU/BUS7
- U44 pad 2: Net-(U44-Pad2) -> Net-(U40-Pad6)
- U44 pad 20: +5V -> GND
- U44 pad 3: Net-(U44-Pad3) -> Net-(U36-Pad9)
- U44 pad 4: Net-(U44-Pad4) -> Net-(U36-Pad8)
- U44 pad 5: Net-(U44-Pad5) -> Net-(U36-Pad7)
- U44 pad 6: Net-(U44-Pad6) -> Net-(U36-Pad6)
- U44 pad 7: Net-(U44-Pad7) -> Net-(U36-Pad5)
- U44 pad 8: Net-(U44-Pad8) -> Net-(U36-Pad4)
- U44 pad 9: Net-(U44-Pad9) -> Net-(U36-Pad3)
- U45 pad 1: /ProgramCounter/~CLR -> (no net)
- U45 pad 10: /ProgramCounter/CE -> Net-(U36-Pad2)
- U45 pad 11: Net-(U43-Pad5) -> /ALU/BUS8
- U45 pad 12: Net-(U43-Pad4) -> /ALU/BUS9
- U45 pad 13: Net-(U43-Pad3) -> /ALU/BUS10
- U45 pad 14: Net-(U43-Pad2) -> GND
- U45 pad 15: Net-(U45-Pad15) -> /ALU/BUS11
- U45 pad 16: +5V -> /ALU/BUS12
- U45 pad 2: /ProgramCounter/CLK -> Net-(U40-Pad6)
- U45 pad 3: /ALU/BUS0 -> Net-(U36-Pad9)
- U45 pad 4: /ALU/BUS1 -> Net-(U36-Pad8)
- U45 pad 5: /ALU/BUS2 -> Net-(U36-Pad7)
- U45 pad 6: /ALU/BUS3 -> Net-(U36-Pad6)
- U45 pad 7: /ProgramCounter/CE -> Net-(U36-Pad5)
- U45 pad 8: GND -> Net-(U36-Pad4)
- U45 pad 9: /ProgramCounter/~J -> Net-(U36-Pad3)
- U46 pad 1: /ProgramCounter/~CLR -> (no net)
- U46 pad 10: /ProgramCounter/CE -> Net-(U36-Pad2)
- U46 pad 11: Net-(U43-Pad9) -> /ALU/BUS0
- U46 pad 12: Net-(U43-Pad8) -> /ALU/BUS1
- U46 pad 13: Net-(U43-Pad7) -> /ALU/BUS2
- U46 pad 14: Net-(U43-Pad6) -> GND
- U46 pad 15: Net-(U46-Pad15) -> /ALU/BUS3
- U46 pad 16: +5V -> /ALU/BUS4
- U46 pad 2: Net-(U45-Pad15) -> Net-(U40-Pad6)
- U46 pad 3: /ALU/BUS4 -> Net-(U36-Pad9)
- U46 pad 4: /ALU/BUS5 -> Net-(U36-Pad8)
- U46 pad 5: /ALU/BUS6 -> Net-(U36-Pad7)
- U46 pad 6: /ALU/BUS7 -> Net-(U36-Pad6)
- U46 pad 7: /ProgramCounter/CE -> Net-(U36-Pad5)
- U46 pad 8: GND -> Net-(U36-Pad4)
- U46 pad 9: /ProgramCounter/~J -> Net-(U36-Pad3)
- U47 pad 1: /ProgramCounter/~CLR -> +5V
- U47 pad 10: /ProgramCounter/CE -> GND
- U47 pad 11: Net-(U44-Pad5) -> /ALU/BUS7
- U47 pad 12: Net-(U44-Pad4) -> /ALU/BUS6
- U47 pad 13: Net-(U44-Pad3) -> /ALU/BUS5
- U47 pad 14: Net-(U44-Pad2) -> /ALU/BUS4
- U47 pad 15: Net-(U47-Pad15) -> /ALU/BUS3
- U47 pad 16: +5V -> /ALU/BUS2
- U47 pad 2: Net-(U46-Pad15) -> /Control Unit/I0
- U47 pad 3: /ALU/BUS8 -> /Control Unit/I1
- U47 pad 4: /ALU/BUS9 -> /Control Unit/I2
- U47 pad 5: /ALU/BUS10 -> /Control Unit/I3
- U47 pad 6: /ALU/BUS11 -> /Control Unit/I4
- U47 pad 7: /ProgramCounter/CE -> /Control Unit/I5
- U47 pad 8: GND -> /Control Unit/I6
- U47 pad 9: /ProgramCounter/~J -> /Control Unit/I7
- U48 pad 1: +5V -> GND
- U48 pad 2: Net-(C4-Pad1) -> GND
- U6 pad 9: (no net) -> Net-(U6-Pad9)
- U7 pad 14: (no net) -> +5V
- U7 pad 7: (no net) -> GND
- U8 pad 14: (no net) -> +5V
- U8 pad 7: (no net) -> GND
- U9 pad 14: (no net) -> +5V
- U9 pad 7: (no net) -> GND
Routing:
- net GND: track 793.5 -> 0.00 mm
- net +5V: track 678.2 -> 0.00 mm
- net /ALU/BUS12: track 433.3 -> 0.00 mm, vias 1 -> 0
- net /ALU/BUS13: track 427.8 -> 0.00 mm, vias 1 -> 0
- net /ALU/BUS8: track 398.9 -> 0.00 mm, vias 1 -> 0
- net /ALU/BUS14: track 395.8 -> 0.00 mm
- net /ALU/BUS5: track 395.0 -> 0.00 mm, vias 3 -> 0
- net /ALU/BUS10: track 382.4 -> 0.00 mm, vias 3 -> 0
- net /ALU/BUS6: track 377.8 -> 0.00 mm, vias 2 -> 0
- net /ALU/BUS11: track 377.0 -> 0.00 mm
- net /ALU/BUS9: track 375.2 -> 0.00 mm, vias 1 -> 0
- net /ALU/BUS4: track 353.2 -> 0.00 mm, vias 5 -> 0
- net /ProgramCounter/CLK: track 351.4 -> 0.00 mm
- net /ALU/BUS7: track 346.4 -> 0.00 mm, vias 1 -> 0
- net /ALU/BUS0: track 338.1 -> 0.00 mm
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
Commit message: Various Fixes
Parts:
- added U53: 74LS173, Package_DIP:DIP-16_W7.62mm, F.Cu at (78.9, 106.4)
- added U54: 74HC02, Package_DIP:DIP-14_W7.62mm, F.Cu at (89.8, 125.8)
- added U55: 74HC02, Package_DIP:DIP-14_W7.62mm, F.Cu at (100.6, 125.8)
- added U56: 74LS08, Package_DIP:DIP-14_W7.62mm, F.Cu at (111.5, 106.4)
- added U57: 74LS08, Package_DIP:DIP-14_W7.62mm, F.Cu at (57.2, 128.3)
- U24: value 74LS08 -> 74LS04
- U26: value 74LS08 -> 74LS32
- moved U31 180.3 mm to (187.7, 106.4)
- moved U18 161.4 mm to (246.8, 58.9), turned to 0 degrees
- moved U32 161.3 mm to (176.8, 106.4)
- moved R6 154.0 mm to (248.4, 177.3)
- moved C1 144.8 mm to (246.4, 151.1)
- moved U33 143.0 mm to (166.0, 106.4)
- moved U19 142.6 mm to (235.9, 58.9), turned to 0 degrees
- moved U27 140.5 mm to (257.1, 156.2)
- moved C4 139.2 mm to (227.8, 157.7)
- moved R3 136.2 mm to (255.2, 167.5)
- moved U28 135.9 mm to (246.2, 156.2)
- moved C2 134.9 mm to (227.8, 144.6)
- moved RV1 134.9 mm to (245.5, 173.4)
- moved SW1 134.9 mm to (217.5, 165.0)
- moved SW2 134.9 mm to (264.8, 145.2)
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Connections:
- net /Control Unit/CLK renamed /ALU/CLK

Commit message: Fixed ZIF
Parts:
- U45, U46: footprint ROM:3M_240-1280-00-0602J -> ROM:ZIF-AT28C64B-15PU
- moved U52 221.0 mm to (41.4, 70.3)
- moved U51 199.8 mm to (52.0, 70.3)
- moved U50 199.8 mm to (20.3, 65.2)
- moved U49 193.8 mm to (52.0, 48.7)
- moved U48 193.5 mm to (41.4, 48.7)
- moved U47 178.8 mm to (30.9, 65.2)
- moved R1 159.6 mm to (130.3, 71.3)
- moved R3 154.2 mm to (130.3, 77.0)
- moved R2 149.0 mm to (130.3, 74.2)
- moved U36 148.8 mm to (89.0, 161.5)
- moved U27 142.1 mm to (130.4, 91.8)
- moved U44 135.5 mm to (70.9, 151.3)
- moved U23 132.3 mm to (130.4, 80.4)
- moved R6 131.7 mm to (159.1, 80.6)
- moved RV1 130.2 mm to (160.0, 75.2)
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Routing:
- net GND: track 0.00 -> 1189.7 mm, vias 0 -> 5
- net +5V: track 0.00 -> 1020.8 mm, vias 0 -> 4
- net /ALU/CLK: track 0.00 -> 510.2 mm, vias 0 -> 10
- net /ALU/BUS1: track 0.00 -> 501.4 mm, vias 0 -> 3
- net /ALU/BUS2: track 0.00 -> 496.4 mm, vias 0 -> 4
- net /ALU/BUS0: track 0.00 -> 481.0 mm, vias 0 -> 4
- net /ALU/BUS3: track 0.00 -> 465.6 mm, vias 0 -> 5
- net /ALU/BUS4: track 0.00 -> 462.6 mm, vias 0 -> 4
- net /ALU/BUS7: track 0.00 -> 454.5 mm, vias 0 -> 4
- net /ALU/BUS10: track 0.00 -> 452.0 mm, vias 0 -> 7
- net /ALU/BUS6: track 0.00 -> 451.9 mm, vias 0 -> 3
- net /ALU/BUS5: track 0.00 -> 450.5 mm, vias 0 -> 4
- net /ALU/BUS11: track 0.00 -> 435.8 mm, vias 0 -> 6
- net /ALU/BUS8: track 0.00 -> 424.0 mm, vias 0 -> 5
- net /ALU/BUS9: track 0.00 -> 422.3 mm, vias 0 -> 3
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
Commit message: Added link for Truth Table
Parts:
- moved R6 145.9 mm to (76.2, 200.7)
- moved U46 136.8 mm to (157.5, 209.6)
- moved U35 127.7 mm to (109.2, 217.2)
- moved R4 125.9 mm to (77.5, 195.6)
- moved U55 122.8 mm to (105.4, 57.1)
- moved U18 111.3 mm to (108.0, 128.3)
- moved R5 109.6 mm to (132.1, 172.7), turned to 180 degrees
- moved U56 109.5 mm to (94.0, 57.1)
- moved U19 108.1 mm to (143.5, 128.3)
- moved U6 97.1 mm to (106.7, 77.5)
- moved C6 95.8 mm to (102.9, 193.0), turned to 90 degrees
- moved RV1 93.4 mm to (134.6, 165.1)
- moved U45 92.6 mm to (132.1, 209.6)
- moved U43 92.6 mm to (67.3, 207.0)
- moved U13 92.0 mm to (156.2, 105.4)
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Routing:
- net GND: track 1189.7 -> 0.00 mm, vias 5 -> 0
- net +5V: track 1020.8 -> 0.00 mm, vias 4 -> 0
- net /ALU/CLK: track 510.2 -> 0.00 mm, vias 10 -> 0
- net /ALU/BUS1: track 501.4 -> 1.59 mm, vias 3 -> 0
- net /ALU/BUS2: track 496.4 -> 1.59 mm, vias 4 -> 0
- net /ALU/BUS0: track 481.0 -> 1.59 mm, vias 4 -> 0
- net /ALU/BUS3: track 465.6 -> 1.59 mm, vias 5 -> 0
- net /ALU/BUS4: track 462.6 -> 0.00 mm, vias 4 -> 0
- net /ALU/BUS7: track 454.5 -> 0.00 mm, vias 4 -> 0
- net /ALU/BUS10: track 452.0 -> 0.00 mm, vias 7 -> 0
- net /ALU/BUS6: track 451.9 -> 0.00 mm, vias 3 -> 0
- net /ALU/BUS5: track 450.5 -> 0.00 mm, vias 4 -> 0
- net /ALU/BUS11: track 435.8 -> 0.00 mm, vias 6 -> 0
- net /ALU/BUS8: track 424.0 -> 0.00 mm, vias 5 -> 0
- net /ALU/BUS9: track 422.3 -> 0.00 mm, vias 3 -> 0
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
